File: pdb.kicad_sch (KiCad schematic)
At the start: 21 parts, among them J1 Amass Elec AS150UPW(2+4), J10 BOOMELE 4.2-2*4AW, J11 MOLEX 39301240, J12 BOOMELE 4.2-2*2AW, J13 BOOMELE 4.2-2*2AW, J14 BOOMELE 4.2-2*3AW, J15 BOOMELE 4.2-2*3AW, J16 BOOMELE 4.2-2*4AW, J17 BOOMELE 4.2-2*2AW, J18 BOOMELE 4.2-2*2AW, J19 BOOMELE 4.2-2*2AW, J2 BOOMELE 4.2-2*3AW, J20 MOLEX 39301240, J3 BOOMELE 4.2-2*3AW, J4 BOOMELE 4.2-2*3AW, J5 BOOMELE 4.2-2*3AW, J6 BOOMELE 4.2-2*4AW, J7 BOOMELE 4.2-2*4AW, J8 BOOMELE 4.2-2*4AW, J9 BOOMELE 4.2-2*4AW

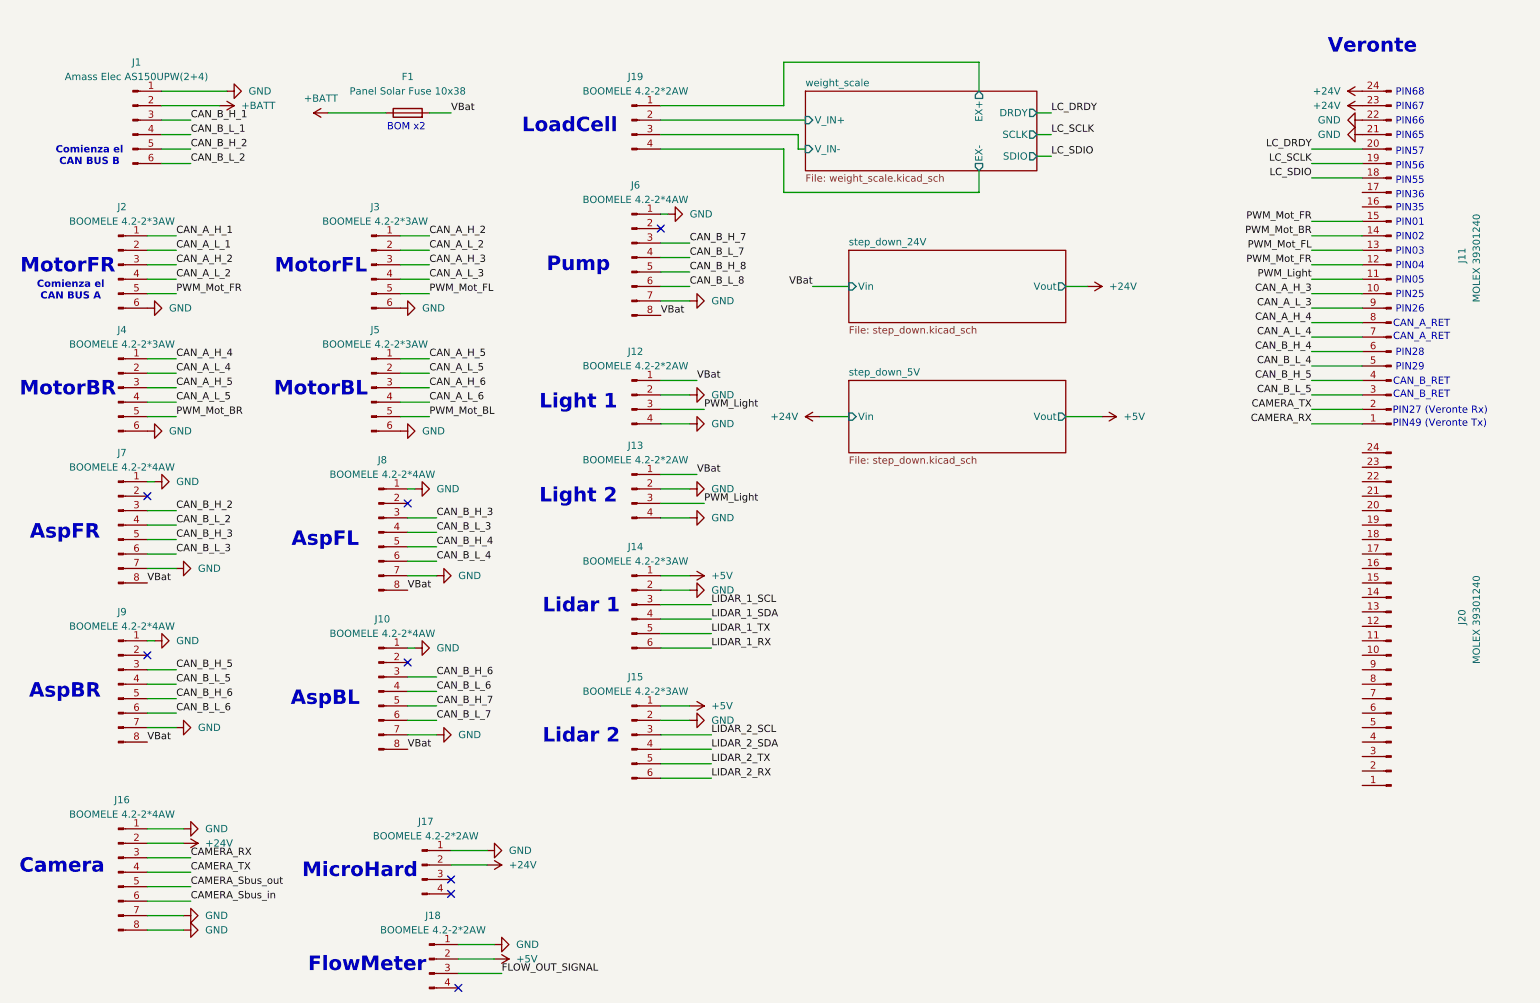
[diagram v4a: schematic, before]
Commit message: ADD: Terminado la fuente de 24V a 5V, terminado los pines del veronte y tambien el circuito de I2C
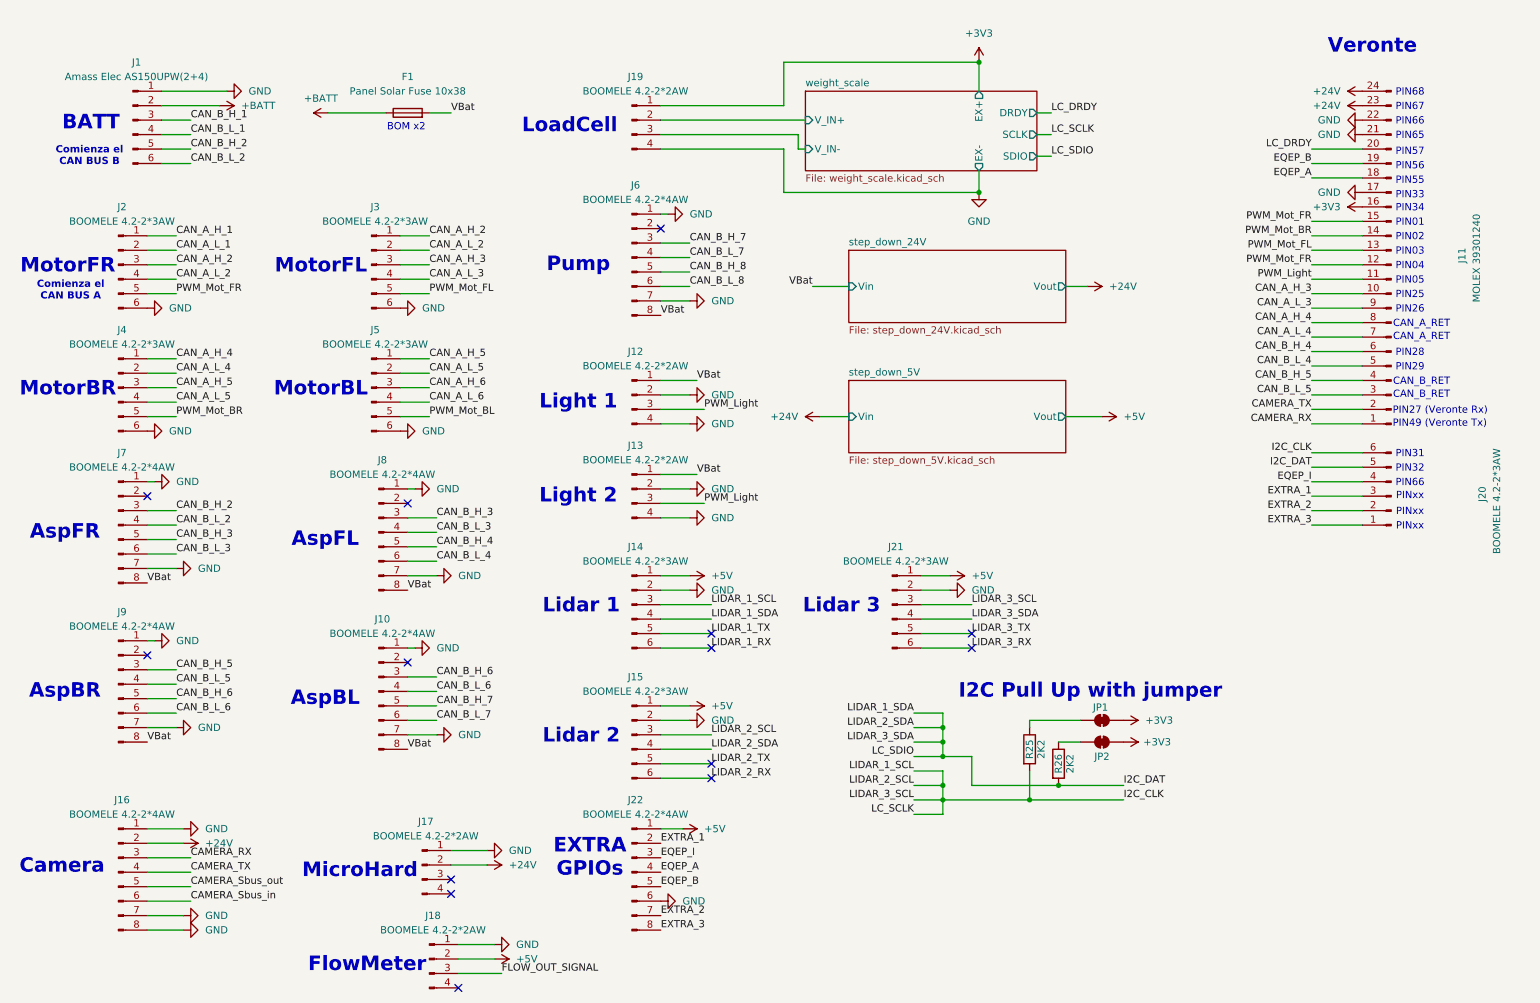
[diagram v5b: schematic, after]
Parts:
- removed J20: MOLEX 39301240, Connector_Molex:Molex_Mini-Fit_Jr_5569-24A2_2x12_P4.20mm_Horizontal, symbol Connector:Conn_01x24_Pin
- added J20, J21: BOOMELE 4.2-2*3AW, Connector_Molex:Molex_Mini-Fit_Jr_5569-06A2_2x03_P4.20mm_Horizontal, symbol Connector:Conn_01x06_Pin
- added J22: BOOMELE 4.2-2*4AW, Connector_Molex:Molex_Mini-Fit_Jr_5569-08A2_2x04_P4.20mm_Horizontal, symbol Connector:Conn_01x08_Pin
- added JP1, JP2: SolderJumper_2_Bridged, Jumper:SolderJumper-2_P1.3mm_Bridged_RoundedPad1.0x1.5mm, symbol Jumper:SolderJumper_2_Bridged
- added R25, R26: 2K2, Resistor_SMD:R_1206_3216Metric, symbol Device:R
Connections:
- net LIDAR_2_SCL is gone; now on net I2C_CLK: J15.3 (Pin_3)
- net LIDAR_2_SDA is gone; now on net I2C_DAT: J15.4 (Pin_4)
- net weight_scale/EX+ is gone; now on net +3V3: J19.1 (Pin_1)
- net weight_scale/EX- is gone; now on net GND: J19.4 (Pin_4)
- net +5V: now also J21.1 (Pin_1), J22.1 (Pin_1)
- net GND: now also J11.17 (Pin_17), J21.2 (Pin_2), J22.6 (Pin_6)
- net +3V3: now reaches J11.16 (Pin_16)
- net +3V3: now also JP1.2 (B), JP2.2 (B)
- net LC_SCLK renamed EQEP_B
- net EQEP_B: now also J22.5 (Pin_5)
- net LC_SDIO renamed EQEP_A
- net EQEP_A: now also J22.4 (Pin_4)
- net LIDAR_1_SCL renamed I2C_CLK
- net I2C_CLK: now also J20.6 (Pin_6), J21.3 (Pin_3), R25.2
- net LIDAR_1_SDA renamed I2C_DAT
- net I2C_DAT: now also J20.5 (Pin_5), J21.4 (Pin_4), R26.2
- new net: JP1.1 (A), R25.1
- new net: JP2.1 (A), R26.1
- new net EQEP_I: J20.4 (Pin_4), J22.3 (Pin_3)
- new net EXTRA_1: J20.3 (Pin_3), J22.2 (Pin_2)
- new net EXTRA_2: J20.2 (Pin_2), J22.7 (Pin_7)
- new net EXTRA_3: J20.1 (Pin_1), J22.8 (Pin_8)
- new net LIDAR_3_RX: J21.6 (Pin_6)
- new net LIDAR_3_TX: J21.5 (Pin_5)
- no-connect marks 8 -> 14
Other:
- sheet step_down_24V: file step_down.kicad_sch -> step_down_24V.kicad_sch
- sheet step_down_5V: file step_down.kicad_sch -> step_down_5V.kicad_sch
- note added: "BATT"
- note added: "EXTRA GPIOs"
- note added: "I2C Pull Up with jumper"
- note added: "Lidar 3"
- note added: "PIN31"
- note added: "PIN32"
- note added: "PIN33"
- note added: "PIN34"
- note added: "PINxx"
- note removed: "PIN35"
- note removed: "PIN36"

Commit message: FIX: Sensor de flujo en EQ
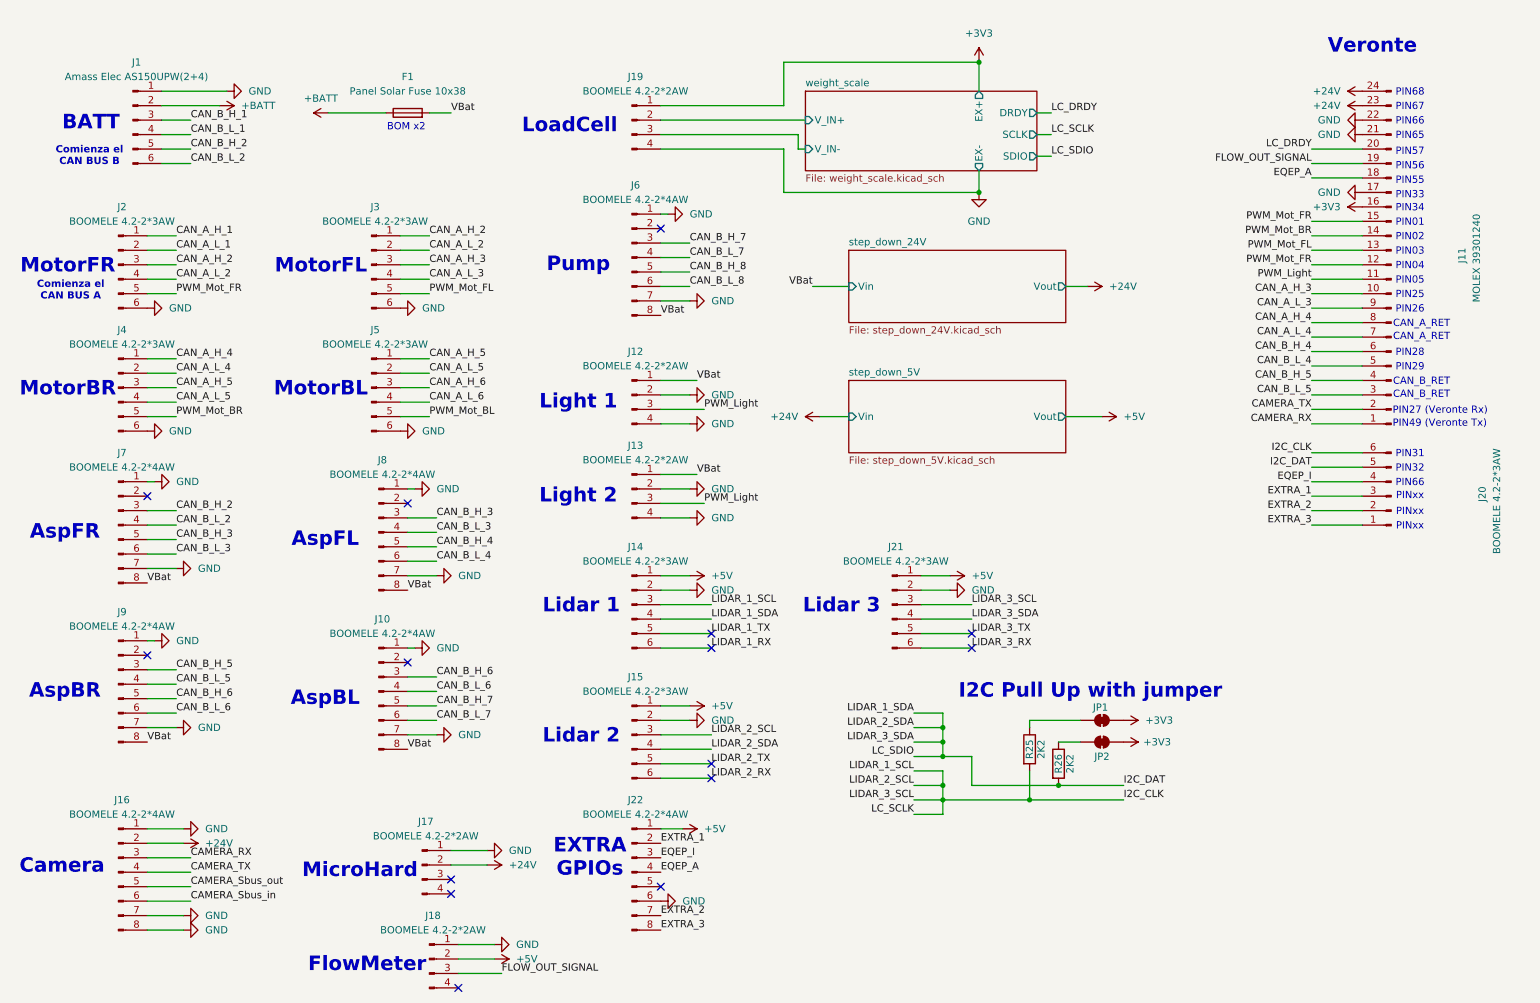
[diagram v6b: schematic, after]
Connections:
- net FLOW_OUT_SIGNAL: now also J11.19 (Pin_19)
- net EQEP_B: no longer names the net of J22.5 (Pin_5)
- net EQEP_B: no longer J11.19 (Pin_19)
- no-connect marks 14 -> 15
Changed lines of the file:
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@@
+	)
+	(no_connect
+		(at 133.35 166.37)
 	)
 	(no_connect
@@
 		)
 	)
-	(label "EQEP_B"
-		(at 247.65 39.37 180)
-		(effects
-			(font
-				(size 1.27 1.27)
-			)
-			(justify right bottom)
-		)
-	)
 	(label "CAN_B_L_2"
 		(at 48.26 102.87 0)
@@
 		)
 	)
-	(label "EQEP_B"
-		(at 133.35 166.37 0)
-		(effects
-			(font
-				(size 1.27 1.27)
-			)
-			(justify left bottom)
-		)
-	)
 	(label "PWM_Light"
 		(at 247.65 59.69 180)
@@
 		)
 	)
+	(label "FLOW_OUT_SIGNAL"
+		(at 247.65 39.37 180)
+		(effects
+			(font
+				(size 1.27 1.27)
+			)
+			(justify right bottom)
+		)
+	)

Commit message: Primer sesion de ruteo
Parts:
- removed J19: BOOMELE 4.2-2*2AW, Connector_Molex:Molex_Mini-Fit_Jr_5569-04A2_2x02_P4.20mm_Horizontal, symbol Connector:Conn_01x04_Pin
- removed JP1, JP2: SolderJumper_2_Bridged, Jumper:SolderJumper-2_P1.3mm_Bridged_RoundedPad1.0x1.5mm, symbol Jumper:SolderJumper_2_Bridged
- added H1, H2, H3, H4, H5: MountingHole_Pad, MountingHole:MountingHole_3.2mm_M3_Pad_Via, symbol Mechanical:MountingHole_Pad
- added J2: BOOMELE 4.2-2*3AW, 0_ZA_Lib:Molex_Mini-Fit_Jr_5569-06A2_2x03_P4.20mm_Horizontal, symbol Connector:Conn_01x06_Pin
- added J23: BOOMELE 4.2-2*4AW, 0_ZA_Lib:Molex_Mini-Fit_Jr_5569-08A2_2x04_P4.20mm_Horizontal, symbol Connector:Conn_01x08_Pin
- added JP1, JP2: SolderJumper_2_Open, Jumper:SolderJumper-2_P1.3mm_Open_TrianglePad1.0x1.5mm, symbol Jumper:SolderJumper_2_Open
- J10: renamed from J13; footprint Connector_Molex:Molex_Mini-Fit_Jr_5569-04A2_2x02_P4.20mm_Horizontal -> 0_ZA_Lib:Molex_Mini-Fit_Jr_5569-04A2_2x02_P4.20mm_Horizontal
- J11: renamed from J20; footprint Connector_Molex:Molex_Mini-Fit_Jr_5569-06A2_2x03_P4.20mm_Horizontal -> 0_ZA_Lib:Molex_Mini-Fit_Jr_5569-06A2_2x03_P4.20mm_Horizontal
- J12: renamed from J7; footprint Connector_Molex:Molex_Mini-Fit_Jr_5569-08A2_2x04_P4.20mm_Horizontal -> 0_ZA_Lib:Molex_Mini-Fit_Jr_5569-08A2_2x04_P4.20mm_Horizontal
- J13: renamed from J8; footprint Connector_Molex:Molex_Mini-Fit_Jr_5569-08A2_2x04_P4.20mm_Horizontal -> 0_ZA_Lib:Molex_Mini-Fit_Jr_5569-08A2_2x04_P4.20mm_Horizontal
- J14: footprint Connector_Molex:Molex_Mini-Fit_Jr_5569-06A2_2x03_P4.20mm_Horizontal -> 0_ZA_Lib:Molex_Mini-Fit_Jr_5569-06A2_2x03_P4.20mm_Horizontal
- J15: renamed from J21; footprint Connector_Molex:Molex_Mini-Fit_Jr_5569-06A2_2x03_P4.20mm_Horizontal -> 0_ZA_Lib:Molex_Mini-Fit_Jr_5569-06A2_2x03_P4.20mm_Horizontal
- J16: renamed from J9; footprint Connector_Molex:Molex_Mini-Fit_Jr_5569-08A2_2x04_P4.20mm_Horizontal -> 0_ZA_Lib:Molex_Mini-Fit_Jr_5569-08A2_2x04_P4.20mm_Horizontal
- J17: renamed from J10; footprint Connector_Molex:Molex_Mini-Fit_Jr_5569-08A2_2x04_P4.20mm_Horizontal -> 0_ZA_Lib:Molex_Mini-Fit_Jr_5569-08A2_2x04_P4.20mm_Horizontal
- J18: renamed from J15; footprint Connector_Molex:Molex_Mini-Fit_Jr_5569-06A2_2x03_P4.20mm_Horizontal -> 0_ZA_Lib:Molex_Mini-Fit_Jr_5569-06A2_2x03_P4.20mm_Horizontal
- J19: renamed from J17; footprint Connector_Molex:Molex_Mini-Fit_Jr_5569-04A2_2x02_P4.20mm_Horizontal -> 0_ZA_Lib:Molex_Mini-Fit_Jr_5569-04A2_2x02_P4.20mm_Horizontal
- J20: renamed from J16; footprint Connector_Molex:Molex_Mini-Fit_Jr_5569-08A2_2x04_P4.20mm_Horizontal -> 0_ZA_Lib:Molex_Mini-Fit_Jr_5569-08A2_2x04_P4.20mm_Horizontal
- J21: renamed from J22; footprint Connector_Molex:Molex_Mini-Fit_Jr_5569-08A2_2x04_P4.20mm_Horizontal -> 0_ZA_Lib:Molex_Mini-Fit_Jr_5569-08A2_2x04_P4.20mm_Horizontal
- J22: renamed from J18; footprint Connector_Molex:Molex_Mini-Fit_Jr_5569-04A2_2x02_P4.20mm_Horizontal -> 0_ZA_Lib:Molex_Mini-Fit_Jr_5569-04A2_2x02_P4.20mm_Horizontal
- J3: renamed from J6; footprint Connector_Molex:Molex_Mini-Fit_Jr_5569-08A2_2x04_P4.20mm_Horizontal -> 0_ZA_Lib:Molex_Mini-Fit_Jr_5569-08A2_2x04_P4.20mm_Horizontal
- J4: renamed from J2; footprint Connector_Molex:Molex_Mini-Fit_Jr_5569-06A2_2x03_P4.20mm_Horizontal -> 0_ZA_Lib:Molex_Mini-Fit_Jr_5569-06A2_2x03_P4.20mm_Horizontal
- J5: renamed from J3; footprint Connector_Molex:Molex_Mini-Fit_Jr_5569-06A2_2x03_P4.20mm_Horizontal -> 0_ZA_Lib:Molex_Mini-Fit_Jr_5569-06A2_2x03_P4.20mm_Horizontal
- J6: renamed from J11; footprint Connector_Molex:Molex_Mini-Fit_Jr_5569-24A2_2x12_P4.20mm_Horizontal -> 0_ZA_Lib:Molex_Mini-Fit_Jr_5569-24A2_2x12_P4.20mm_Horizontal
- J7: renamed from J4; footprint Connector_Molex:Molex_Mini-Fit_Jr_5569-06A2_2x03_P4.20mm_Horizontal -> 0_ZA_Lib:Molex_Mini-Fit_Jr_5569-06A2_2x03_P4.20mm_Horizontal
- J8: renamed from J5; footprint Connector_Molex:Molex_Mini-Fit_Jr_5569-06A2_2x03_P4.20mm_Horizontal -> 0_ZA_Lib:Molex_Mini-Fit_Jr_5569-06A2_2x03_P4.20mm_Horizontal
- J9: renamed from J12; footprint Connector_Molex:Molex_Mini-Fit_Jr_5569-04A2_2x02_P4.20mm_Horizontal -> 0_ZA_Lib:Molex_Mini-Fit_Jr_5569-04A2_2x02_P4.20mm_Horizontal; Function (none) -> Light_1
- renumbered R25 to R1, R26 to R2
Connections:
- net CAN_B_L_8 is gone; now on net GND: J3.6 (Pin_6)
- net +24V: now also J6.11 (Pin_11), J23.8 (Pin_8); no longer J6.24 (Pin_24)
- net +3V3: now also J6.19 (Pin_19), JP1.2 (B), JP2.2 (B); no longer J6.16 (Pin_16)
- net CAMERA_RX: now also J11.4 (Pin_4); no longer J6.1 (Pin_1)
- net CAMERA_TX: now also J11.1 (Pin_1); no longer J6.2 (Pin_2)
- net EQEP_I: now also J6.9 (Pin_9); no longer J11.4 (Pin_4)
- net EXTRA_1: now also J6.6 (Pin_6); no longer J11.3 (Pin_3)
- net EXTRA_2: now also J6.10 (Pin_10); no longer J11.2 (Pin_2)
- net EXTRA_3: now also J6.5 (Pin_5); no longer J11.1 (Pin_1)
- net FLOW_OUT_SIGNAL: now also J22.4 (Pin_4), J6.16 (Pin_16); no longer J22.3 (Pin_3), J6.19 (Pin_19)
- net GND: now also J10.3 (Pin_3), J12.6 (Pin_6), J13.6 (Pin_6), J16.6 (Pin_6), J17.6 (Pin_6), J9.3 (Pin_3), J2.1 (Pin_1), J2.2 (Pin_2), J2.3 (Pin_3), J23.6 (Pin_6), J23.7 (Pin_7); no longer J10.2 (Pin_2), J12.1 (Pin_1), J13.1 (Pin_1), J16.1 (Pin_1), J17.1 (Pin_1), J3.1 (Pin_1), J9.2 (Pin_2)
- net I2C_CLK: now also J14.5 (Pin_5), J15.4 (Pin_4), J18.5 (Pin_5), J6.12 (Pin_12); no longer J11.6 (Pin_6), J14.3 (Pin_3), J15.3 (Pin_3), J18.3 (Pin_3)
- net I2C_DAT: now also J15.5 (Pin_5), J6.24 (Pin_24); no longer J11.5 (Pin_5), J15.4 (Pin_4)
- net LIDAR_1_TX: now also J14.3 (Pin_3); no longer J14.5 (Pin_5)
- net LIDAR_2_TX: now also J18.3 (Pin_3); no longer J18.5 (Pin_5)
- net LIDAR_3_TX: now also J15.3 (Pin_3); no longer J15.5 (Pin_5)
- net PWM_Light: now also J10.2 (Pin_2), J6.4 (Pin_4), J9.2 (Pin_2); no longer J10.3 (Pin_3), J6.11 (Pin_11), J9.3 (Pin_3)
- net PWM_Mot_BL: now also J11.5 (Pin_5)
- net PWM_Mot_BR: now also J6.3 (Pin_3); no longer J6.14 (Pin_14)
- net PWM_Mot_FL: now also J11.2 (Pin_2); no longer J6.13 (Pin_13)
- net PWM_Mot_FR: no longer J6.12 (Pin_12)
- net weight_scale/V_IN+: now also J2.4 (Pin_4)
- net weight_scale/V_IN-: now also J2.5 (Pin_5)
- net CAN_B_-_7: now reaches J17.2 (Pin_2)
- net CAN_B_-_7: now also J11.3 (Pin_3)
- net CAN_B_-_6: now reaches J13.2 (Pin_2)
- net CAN_B_-_6: now also J17.3 (Pin_3)
- net CAN_B_-_9: now reaches J16.2 (Pin_2)
- net CAN_B_-_3: now reaches J3.2 (Pin_2)
- net CAN_B_-_3: now also J23.3 (Pin_3)
- net at R1.1: now also JP1.1 (A)
- net at R2.1: now also JP2.1 (A)
- net CAN_B_-_5: now reaches J12.2 (Pin_2)
- net CAN_B_-_5: now also J13.3 (Pin_3)
- net CAN_A_H_1 renamed CAN_A_-_3
- net CAN_A_-_3: now also J5.2 (Pin_2)
- net CAN_A_H_2 renamed CAN_A_+_2
- net CAN_A_+_2: now also J7.4 (Pin_4); no longer J5.1 (Pin_1)
- net CAN_A_H_3 renamed CAN_A_+_3
- net CAN_A_+_3: now also J4.4 (Pin_4); no longer J6.10 (Pin_10)
- net CAN_A_H_4: no longer names the net of J6.8 (Pin_8)
- net CAN_A_H_4: no longer J7.1 (Pin_1)
- net CAN_A_H_5 renamed CAN_A_+_1
- net CAN_A_+_1: now also J6.13 (Pin_13); no longer J8.1 (Pin_1)
- net CAN_A_H_6 renamed CAN_A_+_4
- net CAN_A_+_4: now also J5.4 (Pin_4)
- net CAN_A_L_1 renamed CAN_A_-_2
- net CAN_A_-_2: now also J7.1 (Pin_1)
- removed net CAN_A_L_2: J4.4 (Pin_4), J5.2 (Pin_2)
- removed net CAN_A_L_3: J5.4 (Pin_4), J6.9 (Pin_9)
- net CAN_A_L_4: no longer names the net of J6.7 (Pin_7)
- net CAN_A_L_4: no longer J7.2 (Pin_2)
- net CAN_A_L_5 renamed CAN_A_-_4
- net CAN_A_-_4: now also J5.1 (Pin_1); no longer J7.4 (Pin_4)
- net CAN_A_L_6 renamed CAN_A_+_5
- net CAN_B_H_1 renamed CAN_B_+_2
- net CAN_B_+_2: now also J3.4 (Pin_4)
- net CAN_B_H_2 renamed CAN_B_+_1
- net CAN_B_+_1: no longer J12.3 (Pin_3)
- net CAN_B_H_3: no longer names the net of J12.5 (Pin_5)
- net CAN_B_H_3: no longer J13.3 (Pin_3)
- net CAN_B_H_4: no longer names the net of J13.5 (Pin_5)
- net CAN_B_H_4: no longer J6.6 (Pin_6)
- net CAN_B_H_5 renamed CAN_B_-_8
- net CAN_B_-_8: now also J6.2 (Pin_2); no longer J6.4 (Pin_4)
- net CAN_B_H_6: no longer names the net of J16.5 (Pin_5)
- net CAN_B_H_6: no longer J17.3 (Pin_3)
- net CAN_B_H_7: no longer names the net of J17.5 (Pin_5)
- net CAN_B_H_7: no longer J3.3 (Pin_3)
- net CAN_B_H_8: no longer names the net of J3.5 (Pin_5)
- net CAN_B_L_1 renamed CAN_B_-_2
- net CAN_B_-_2: now also J3.3 (Pin_3)
- net CAN_B_L_2 renamed CAN_B_+_4
- net CAN_B_+_4: now also J23.1 (Pin_1); no longer J1.6 (Pin_6)
- net CAN_B_L_3 renamed CAN_B_+_5
- net CAN_B_+_5: now also J12.1 (Pin_1); no longer J12.6 (Pin_6)
- removed net CAN_B_L_4: J13.6 (Pin_6), J6.5 (Pin_5)
- net CAN_B_L_5 renamed CAN_B_+_8
- net CAN_B_+_8: now also J6.14 (Pin_14); no longer J6.3 (Pin_3)
- net CAN_B_L_6 renamed CAN_B_+_6
- net CAN_B_+_6: now also J13.1 (Pin_1); no longer J16.6 (Pin_6)
- removed net CAN_B_L_7: J17.6 (Pin_6), J3.4 (Pin_4)
- new net CAN_A_-_1: J6.1 (Pin_1), J7.2 (Pin_2)
- new net CAN_A_-_5: J8.1 (Pin_1)
- new net CAN_B_+_3: J23.4 (Pin_4), J3.1 (Pin_1)
- new net CAN_B_+_7: J11.6 (Pin_6), J17.1 (Pin_1)
- new net CAN_B_+_9: J16.1 (Pin_1)
- new net CAN_B_-_1: J1.6 (Pin_6)
- new net CAN_B_-_4: J12.3 (Pin_3), J23.2 (Pin_2)
- new net weight_scale/EX+: J2.6 (Pin_6)
- no-connect marks 15 -> 23
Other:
- sheet weight_scale ports: added VDD; removed none
- note added: "MEX"
- note added: "RET CAN +"
- note added: "RET CAN -"
- note added: "pDDL"
- note removed: "CAN_B_RET"
- note removed: "MicroHard"
